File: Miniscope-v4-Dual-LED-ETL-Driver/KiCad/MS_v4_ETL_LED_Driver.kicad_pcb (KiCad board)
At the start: 6 copper layers, 9.7 x 10.5 mm, 32 parts, among them J1 Conn_01x01, J10 Conn_01x05, J6 Conn_01x01, J7 Conn_01x01, U1 MAX14574EWL+, U2 TPL0102-100RUCR, U3 LTC3218, U4 LTC3218

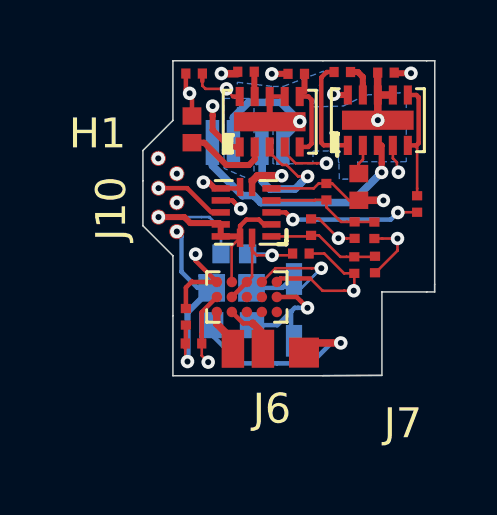
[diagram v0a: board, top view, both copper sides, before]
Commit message: Correct minor trace and silk issues. Generate Gerbers for JLCPCB order
This is the commit connected to the first JLCPCB PCB fab on 6/16/2019.
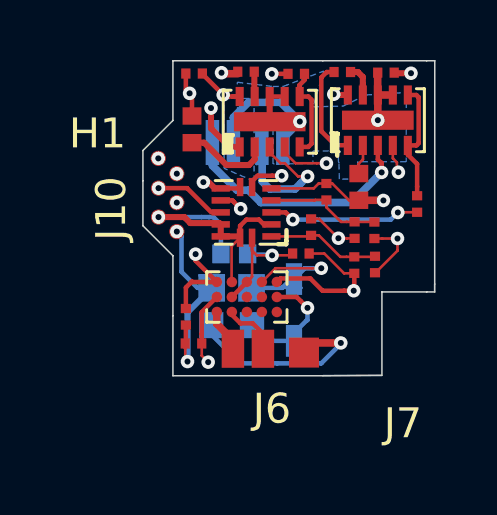
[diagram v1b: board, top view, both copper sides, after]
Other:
- rule solder_mask_min_width: 0.25 -> 0.0762
- board text removed: "P2"

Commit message: Schematics update
Changes:

* Removed the pull-up 3k3 resistors in the I2C lines and replaced the with DNL value.
* Added the correct values for the voltage divider resistors

To do

* Fix the I2C resistors in the release board (wrongly placed as 10k2 resistors)
* Fix the position of LEDs and add two screws for better alignment
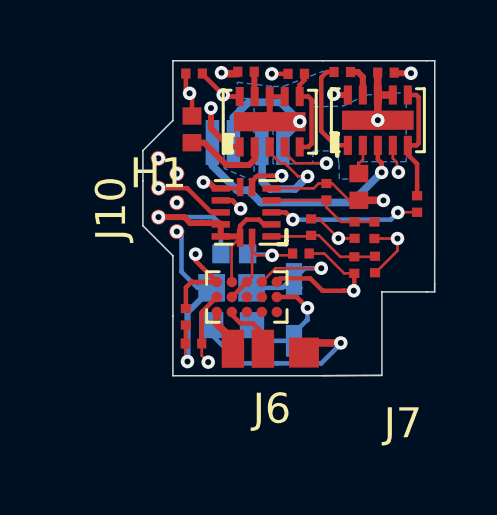
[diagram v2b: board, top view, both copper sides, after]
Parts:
- R5, R7: value 8k2 -> ERJ-1GNJ622C
- R6, R8: value 4k7 -> ERJ-1GEF3741C
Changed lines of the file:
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@@
-(kicad_pcb (version 20171130) (host pcbnew "(5.1.0)-1")
+(kicad_pcb (version 20171130) (host pcbnew "(5.1.2)-1")
   (general
     (thickness 0.8)
@@
   )
   (setup
-    (last_trace_width 0.152)
+    (last_trace_width 0.0889)
     (user_trace_width 0.09)
     (user_trace_width 0.1016)
@@
     (add_net "Net-(U1-PadC5)")
   )
+  (module .Connector:Conn_1x1_700_Circular_Pad (layer F.Cu)
+    (at 12.79652 16.53794)
+    (fp_text reference H1 (at 0 0.5) (layer F.SilkS)
+      (effects (font (size 1 1) (thickness 0.15)))
+    )
+    (fp_text value MountingHole_Pad (at 0 -0.5) (layer F.Fab)
+      (effects (font (size 1 1) (thickness 0.15)))
+    )
+    (pad 1 smd circle (at 0 0) (size 0.508 0.508) (layers F.Cu F.Paste F.Mask)
+      (net 24 /ENT2))
+  )
   (module .LED:LED_LXZ1_PR01_L (layer B.Cu)
     (at 16.5992 16.0092)
@@
       (rotate (xyz -90 0 0))
     )
-  )
-  (module .Connector:Conn_1x1_700_Circular_Pad (layer F.Cu)
-    (at 12.79652 16.53794)
-    (fp_text reference H1 (at -2.02652 -0.82794) (layer F.SilkS)
-      (effects (font (size 1 1) (thickness 0.15)))
-    )
-    (fp_text value MountingHole_Pad (at 0 -0.5) (layer F.Fab)
-      (effects (font (size 1 1) (thickness 0.15)))
-    )
-    (fp_circle (center 0 0) (end 0.3 0) (layer F.CrtYd) (width 0.05))
-    (pad 1 smd circle (at 0 0) (size 0.508 0.508) (layers F.Cu F.Paste F.Mask)
-      (net 24 /ENT2))
   )
   (module .Diode:SOD_323_250X125X110L30X32L (layer B.Cu)
@@
       (effects (font (size 1 1) (thickness 0.1)))
     )
-    (fp_text value 8k2 (at 0 0 90) (layer F.Fab)
+    (fp_text value ERJ-1GNJ622C (at 0 0 90) (layer F.Fab)
       (effects (font (size 1.2 1.2) (thickness 0.12)))
     )
@@
       (effects (font (size 1 1) (thickness 0.1)))
     )
-    (fp_text value 4k7 (at 0 0 90) (layer F.Fab)
+    (fp_text value ERJ-1GEF3741C (at 0 0 90) (layer F.Fab)
       (effects (font (size 1.2 1.2) (thickness 0.12)))
     )
@@
       (effects (font (size 1 1) (thickness 0.1)))
     )
-    (fp_text value 8k2 (at 0 0 90) (layer F.Fab)
+    (fp_text value ERJ-1GNJ622C (at 0 0 90) (layer F.Fab)
       (effects (font (size 1.2 1.2) (thickness 0.12)))
     )
@@
       (effects (font (size 1 1) (thickness 0.1)))
     )
-    (fp_text value 4k7 (at 0 0 90) (layer F.Fab)
-      (effects (font (size 1.2 1.2) (thickness 0.12)))
-    )
+    (fp_text value ERJ-1GEF3741C (at 0 0 90) (layer F.Fab)
+      (effects (font (size 1.2 1.2) (thickness 0.12)))
+    )
